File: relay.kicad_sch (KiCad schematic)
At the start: 14 parts, among them K3501 ALFG2PF12, Q3501 DPLS350E

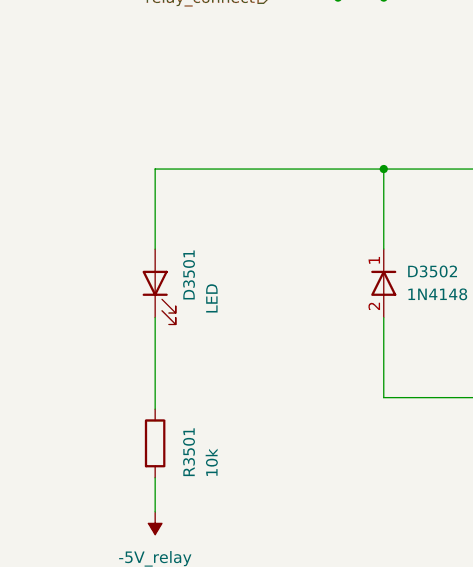
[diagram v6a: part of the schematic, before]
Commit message: add pss lightpipe to schematic
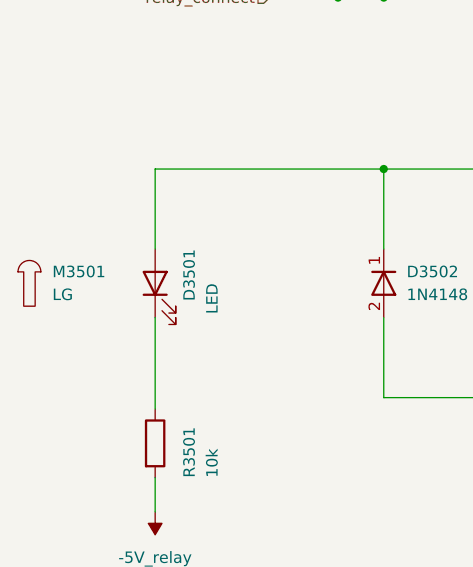
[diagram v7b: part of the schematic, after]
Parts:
- added M3501: LG, symbol pss:Lightguide_D4mm_L22.86mm_Dout5mm
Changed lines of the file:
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@@
 		(title "Power Supply Sink")
 		(date "2024-12-10")
-		(rev "0.13.9")
+		(rev "0.14.0")
 		(company "Open Battery Tester")
 		(comment 1 "Relay")
@@
 					(unit 1)
 				)
+			)
+		)
+	)
+	(symbol
+		(lib_id "pss:Lightguide_D4mm_L22.86mm_Dout5mm")
+		(at 77.47 114.3 0)
+		(unit 1)
+		(exclude_from_sim yes)
+		(in_bom yes)
+		(on_board no)
+		(dnp no)
+		(fields_autoplaced yes)
+		(property "Reference" "M3501"
+			(at 80.01 113.0299 0)
+			(effects
+				(font
+					(size 1.27 1.27)
+				)
+				(justify left)
+			)
+		)
+		(property "Value" "LG"
+			(at 80.01 115.5699 0)
+			(effects
+				(font
+					(size 1.27 1.27)
+				)
+				(justify left)
+			)
+		)
+		(property "Footprint" ""
+			(at 77.47 114.3 0)
+			(effects
+				(font
+					(size 1.27 1.27)
+				)
+				(hide yes)
+			)
+		)
+		(property "Datasheet" "./datasheet/Dialight_12192017_Panel-Mount-5mm-Lightpipe-1272673.pdf"
+			(at 77.47 114.3 0)
+			(effects
+				(font
+					(size 1.27 1.27)
+				)
+				(hide yes)
+			)
+		)
+		(property "Description" "Panel Mount 5mm Lightpipe, Mountinghole 4mm, Length 22.86mm"
+			(at 77.47 114.3 0)
+			(effects
+				(font
+					(size 1.27 1.27)
+				)
+				(hide yes)
+			)
+		)
+		(property "MPN" "51513510900F"
+			(at 77.47 114.3 0)
+			(effects
+				(font
+					(size 1.27 1.27)
+				)
+				(hide yes)
+			)
+		)
+		(property "VPN" "645-51513510900F"
+			(at 77.47 114.3 0)
+			(effects
+				(font
+					(size 1.27 1.27)
+				)
+				(hide yes)
+			)
+		)
+		(instances
+			(project "pss"
+				(path "/3c438cf7-9350-4e9f-8115-1deba8984176/8c067982-1bdd-455d-9e35-2bb5ebdf1fda"
+					(reference "M3501")
+					(unit 1)
+				)

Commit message: fix pss lightpipe length variant selection
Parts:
- M3501: MPN 51513510900F -> 51513510188F; VPN 645-51513510900F -> 645-51513510188F
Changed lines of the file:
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@@
 			)
 		)
-		(property "MPN" "51513510900F"
+		(property "MPN" "51513510188F"
 			(at 77.47 114.3 0)
 			(effects
@@
 			)
 		)
-		(property "VPN" "645-51513510900F"
+		(property "VPN" "645-51513510188F"
 			(at 77.47 114.3 0)
 			(effects
